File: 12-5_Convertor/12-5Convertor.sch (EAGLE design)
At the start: 14 parts, among them IC1 ACS764, U1 LM2678

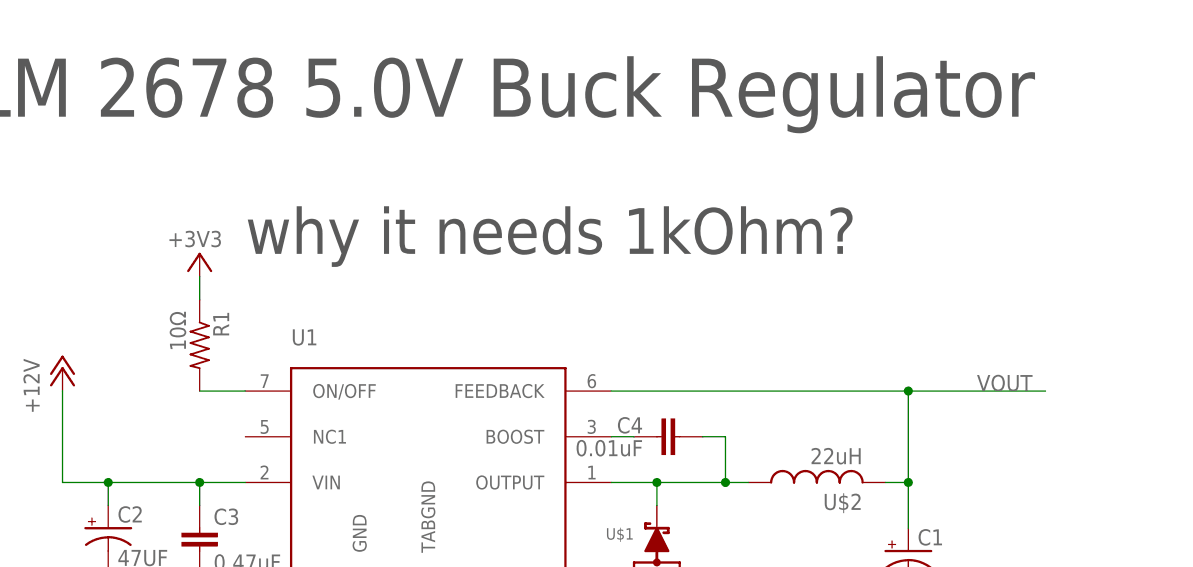
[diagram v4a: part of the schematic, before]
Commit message: "Added Richard's updated version of the buck converter board"
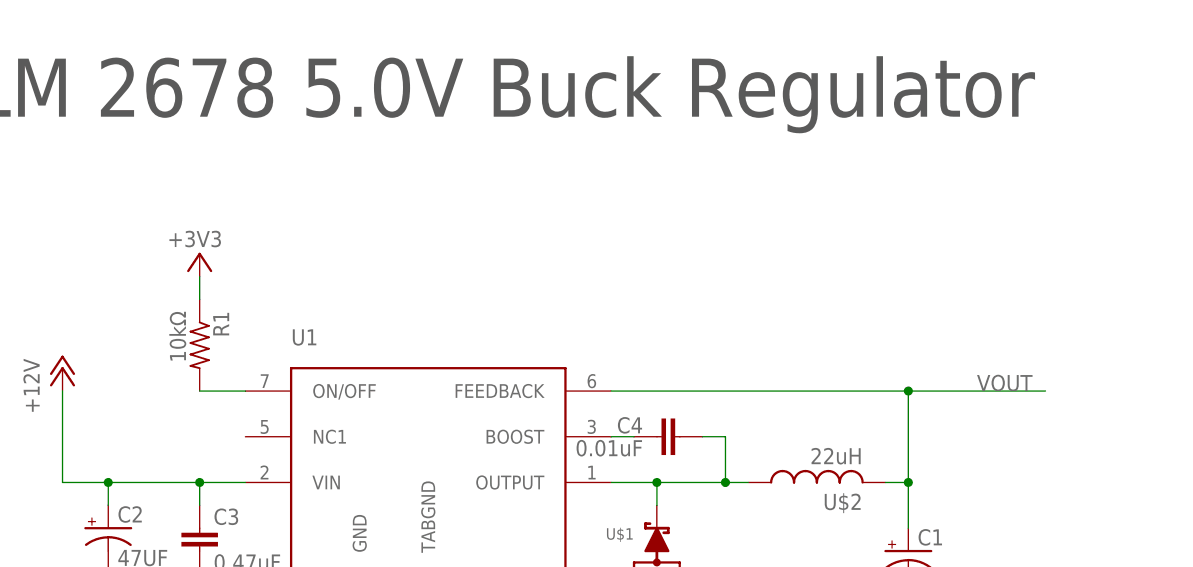
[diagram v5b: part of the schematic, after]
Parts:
- R1: value 10Ω -> 10kΩ
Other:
- note removed: "why it needs 1kOhm?"
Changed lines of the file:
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@@
 <part name="C7" library="SparkFun-Passives" deviceset="CAP" device="0603-CAP" value="1uF"/>
 <part name="C8" library="SparkFun-Passives" deviceset="CAP" device="0603-CAP" value="1uF"/>
-<part name="R1" library="DiscreteComponents" deviceset="R-US_" device="R0603" value="10Ω"/>
+<part name="R1" library="DiscreteComponents" deviceset="R-US_" device="R0603" value="10kΩ"/>
 <part name="IC1" library="ACS764" deviceset="ACS764" device=""/>
 <part name="GND3" library="SparkFun-Aesthetics" deviceset="GND" device=""/>
@@
 <text x="38.1" y="195.58" size="6.4516" layer="97">Current Sensor
 Output is I2C signal</text>
-<text x="40.64" y="63.5" size="5.08" layer="97">why it needs 1kOhm?</text>
 </plain>
 <instances>

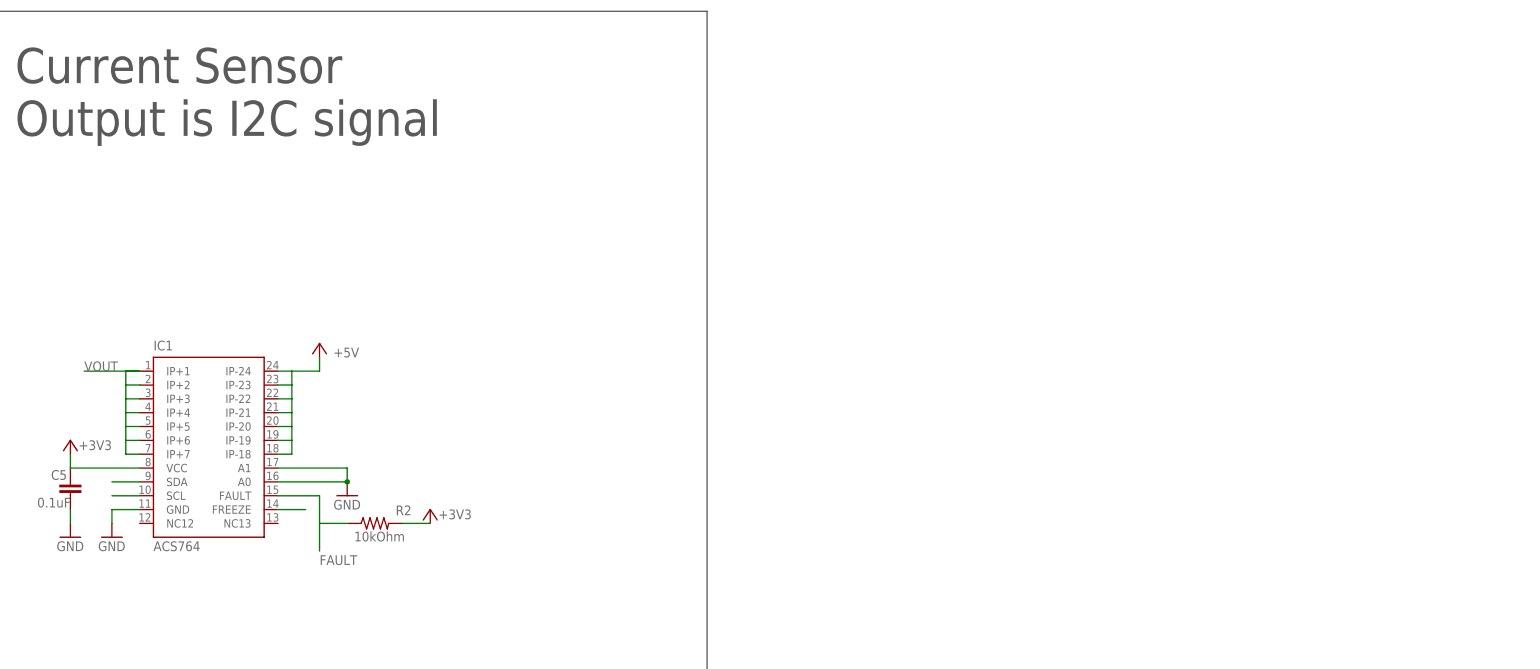
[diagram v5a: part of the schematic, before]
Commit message: Added the board edge connector
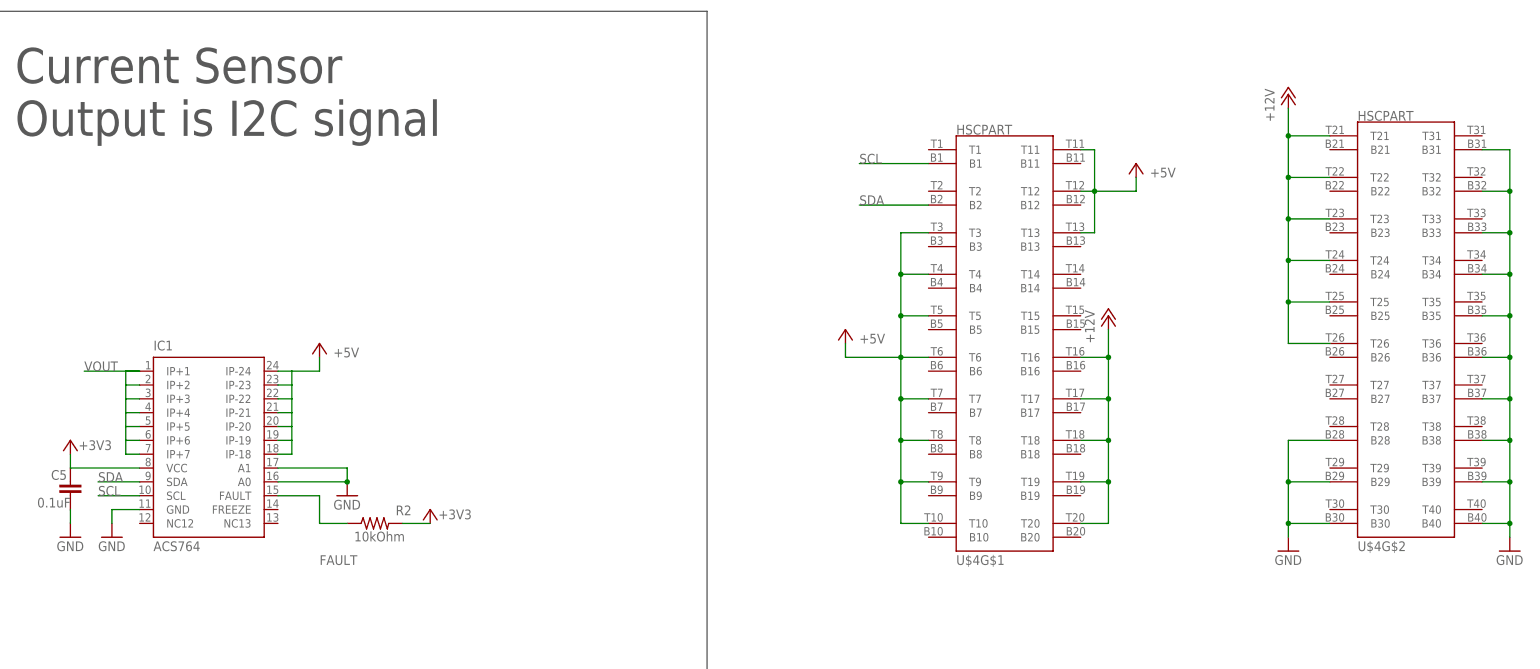
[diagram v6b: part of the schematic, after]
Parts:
- added U$4: HSCPART, Connectors:HSCPART
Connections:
- removed net N$10: IC1.FREEZE
- removed net N$11: IC1.SDA
- removed net N$12: IC1.SCL
- new net SCL: IC1.SCL, U$4G$1.B1
- new net SDA: IC1.SDA, U$4G$1.B2
- net +12V: now also U$4G$1.T16, U$4G$1.T17, U$4G$1.T18, U$4G$1.T19, U$4G$1.T20, U$4G$2.T21, U$4G$2.T22, U$4G$2.T23, U$4G$2.T24, U$4G$2.T25, U$4G$2.T26
- net +5V: now also U$4G$1.T10, U$4G$1.T11, U$4G$1.T12, U$4G$1.T13, U$4G$1.T3, U$4G$1.T4, U$4G$1.T5, U$4G$1.T6, U$4G$1.T7, U$4G$1.T8, U$4G$1.T9
- net GND: now also U$4G$2.B28, U$4G$2.B29, U$4G$2.B30, U$4G$2.B31, U$4G$2.B32, U$4G$2.B33, U$4G$2.B34, U$4G$2.B35, U$4G$2.B36, U$4G$2.B37, U$4G$2.B38, U$4G$2.B39, U$4G$2.B40

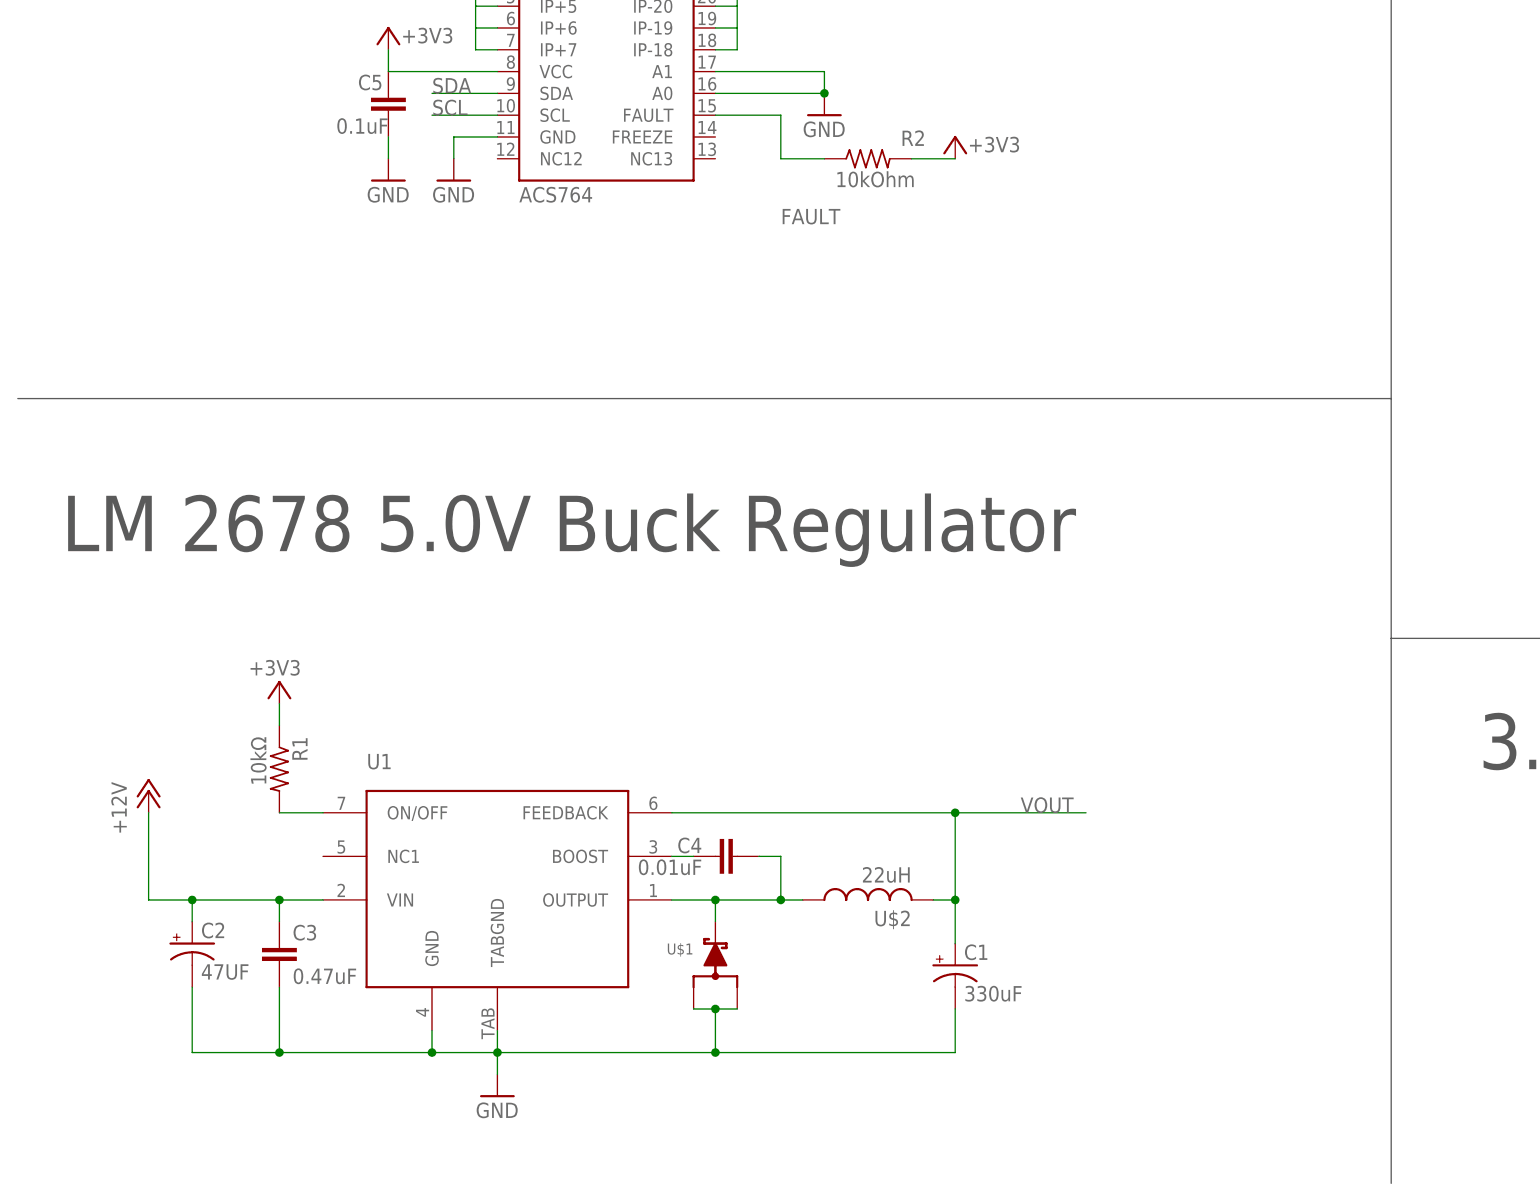
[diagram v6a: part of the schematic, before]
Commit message: Added tantalum capacitors to buck regulator board
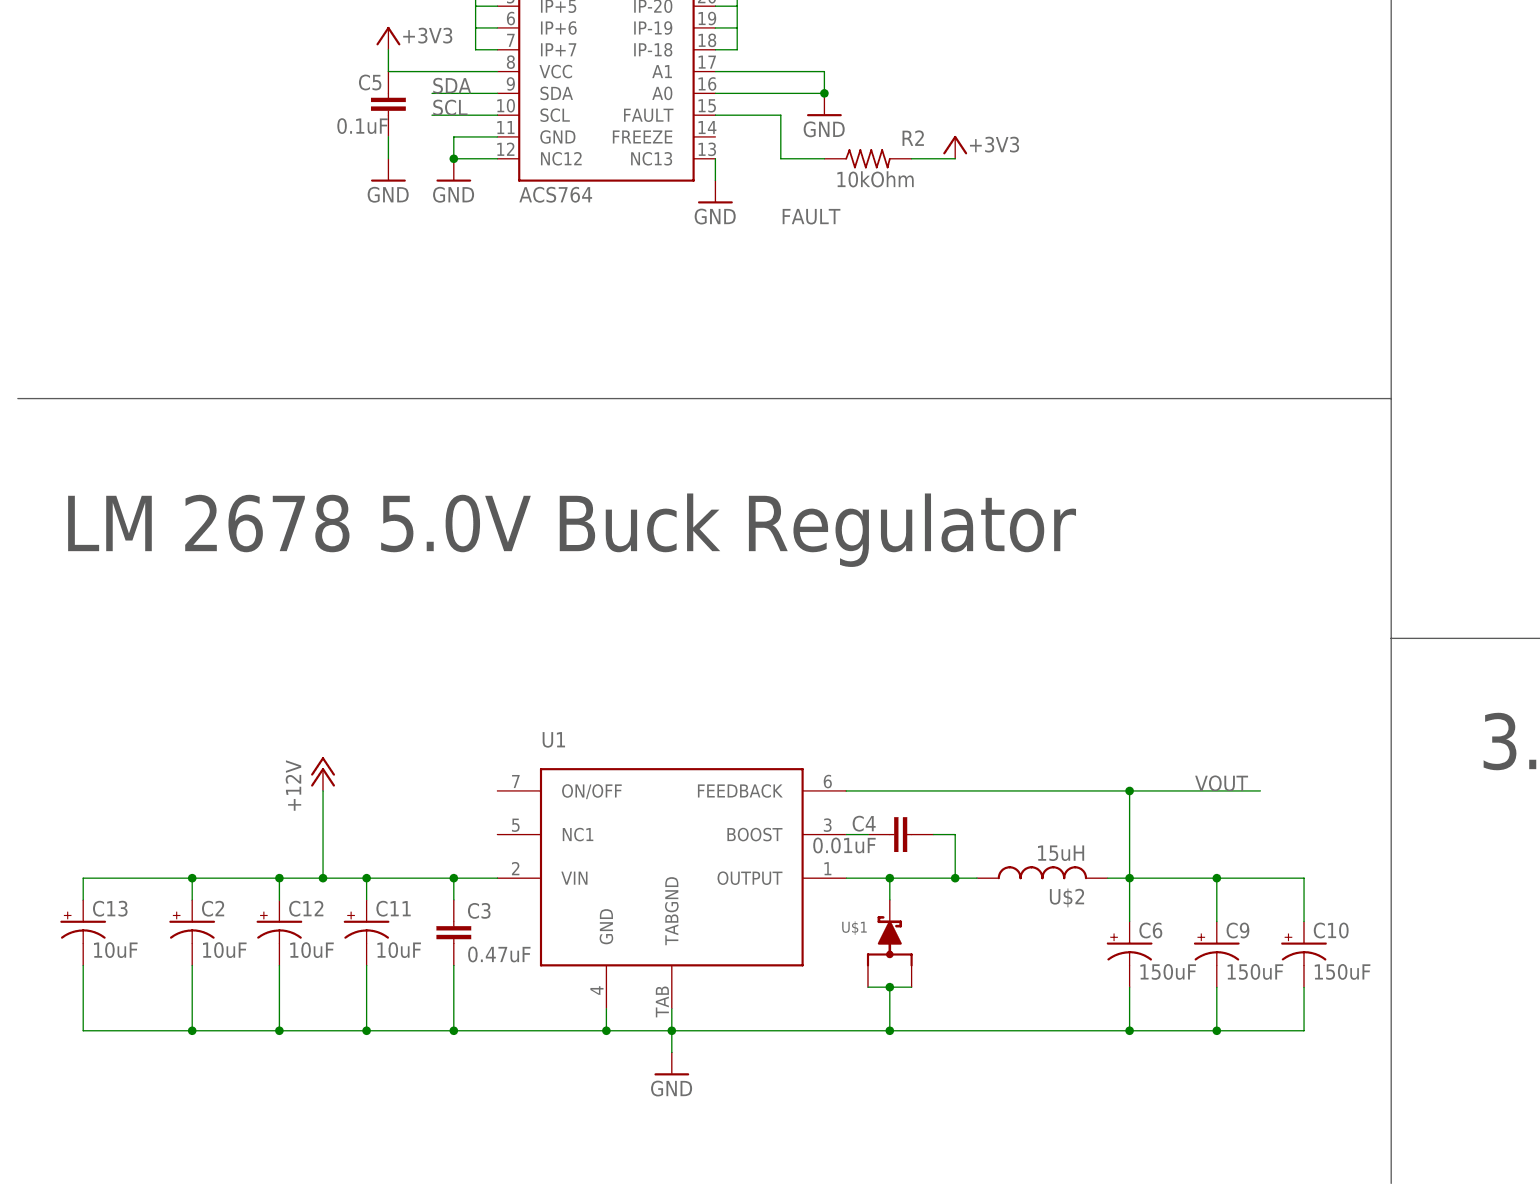
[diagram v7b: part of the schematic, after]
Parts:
- removed C1: 330uF, PowerComponents:C-ALUMINUM(330UF)
- removed R1: 10kΩ, DiscreteComponents:R-US_R0603
- added C10, C6, C9: 150uF, PowerComponents:C-TANTALUM(10UF_150UF)
- added C11, C12, C13: 10uF, PowerComponents:C-TANTALUM(10UF_150UF)
- C2: value 47UF -> 10uF; device PowerComponents:C-ALUMINUM(47UF) -> PowerComponents:C-TANTALUM(10UF_150UF)
- U$2: value 22uH -> 15uH
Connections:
- removed net N$5: R1.2, U1.ON/OFF
- net +12V: now also C11.+, C12.+, C13.+
- net +3V3: no longer R1.1
- net GND: now also C10.-, C11.-, C12.-, C13.-, C6.-, C9.-, IC1.NC12, IC1.NC13; no longer C1.-
- net VOUT: now also C10.+, C6.+, C9.+; no longer C1.+
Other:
- moved on the sheet: C2, C3, C4, U$1, U$2, U1
